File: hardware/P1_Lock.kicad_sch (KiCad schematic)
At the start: 5 parts, among them J1 Conn_01x07, U1 STM32L476RGTx

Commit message: Columns are 1-4
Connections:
- net at J1.4 (Pin_4): now also U1.41 (PA8)
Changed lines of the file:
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@@
+	(wire
+		(pts
+			(xy 144.78 74.93) (xy 152.4 74.93)
+		)
+		(stroke
+			(width 0)
+			(type default)
+		)
+	)
 	(wire
 		(pts
@@
 		(pts
 			(xy 187.96 107.95) (xy 160.02 107.95)
+		)
+		(stroke
+			(width 0)
+			(type default)
+		)
+	)
+	(wire
+		(pts
+			(xy 187.96 115.57) (xy 152.4 115.57)
 		)
 		(stroke
@@
 		)
 		(stroke
+			(width 0)
+			(type default)
+		)
+	)
+	(wire
+		(pts
+			(xy 152.4 115.57) (xy 152.4 74.93)
+		)
+		(stroke

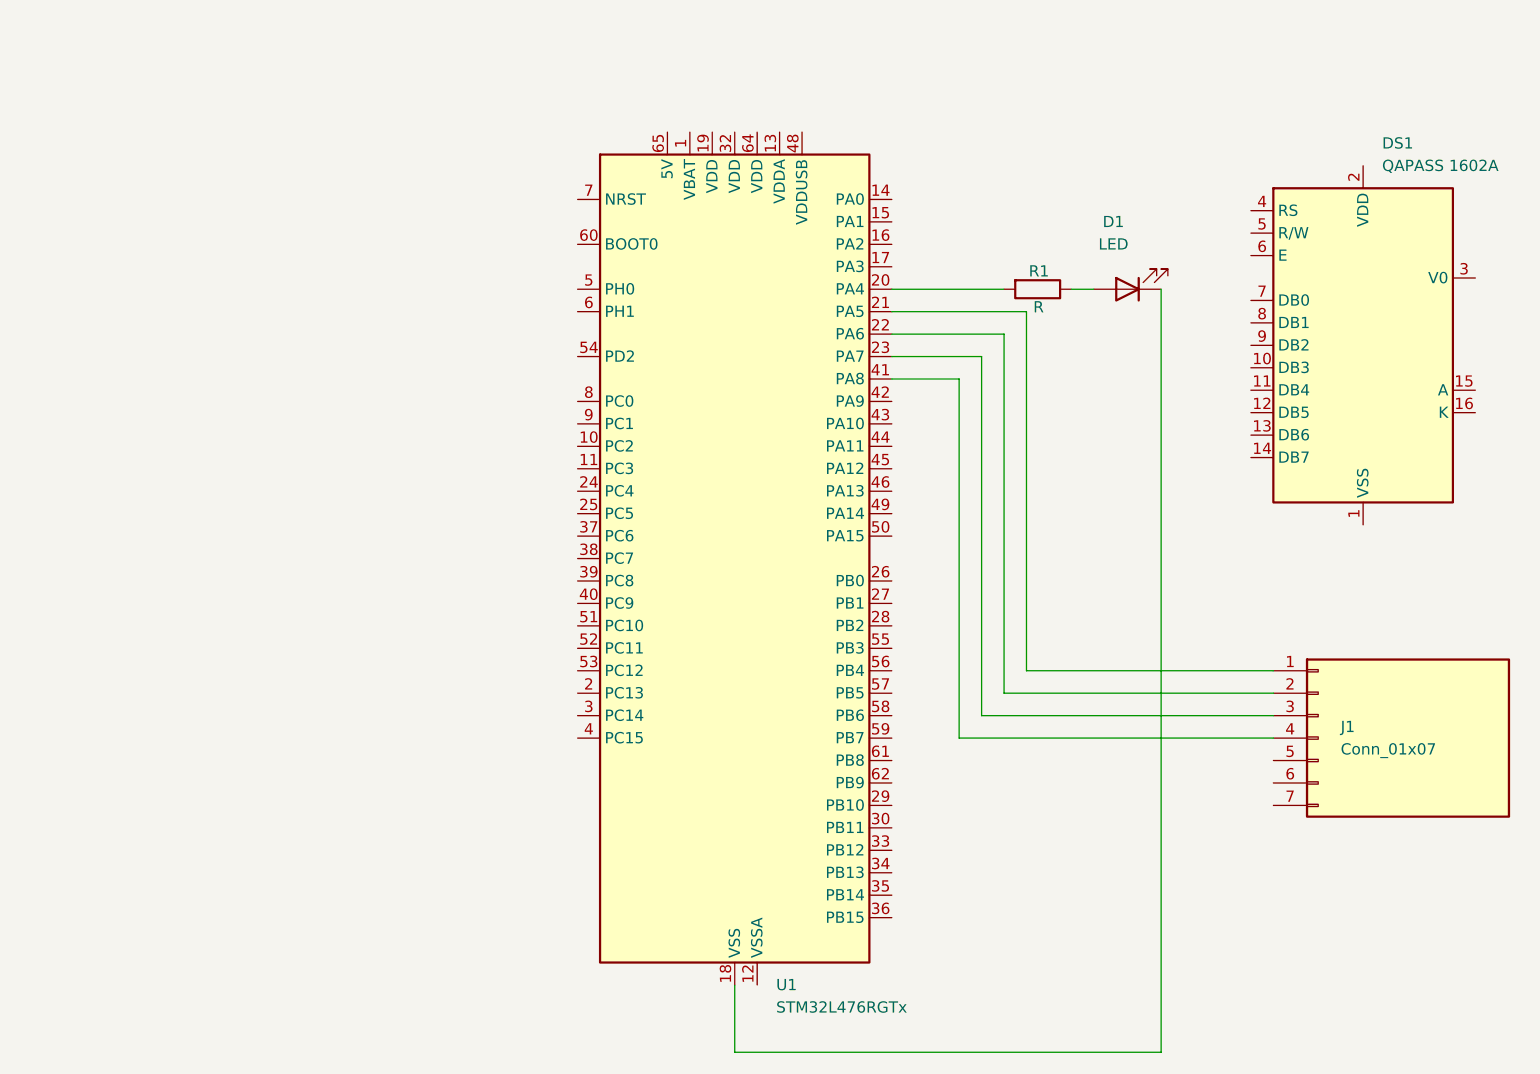
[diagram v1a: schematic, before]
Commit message: LCD Panel complete hooked up
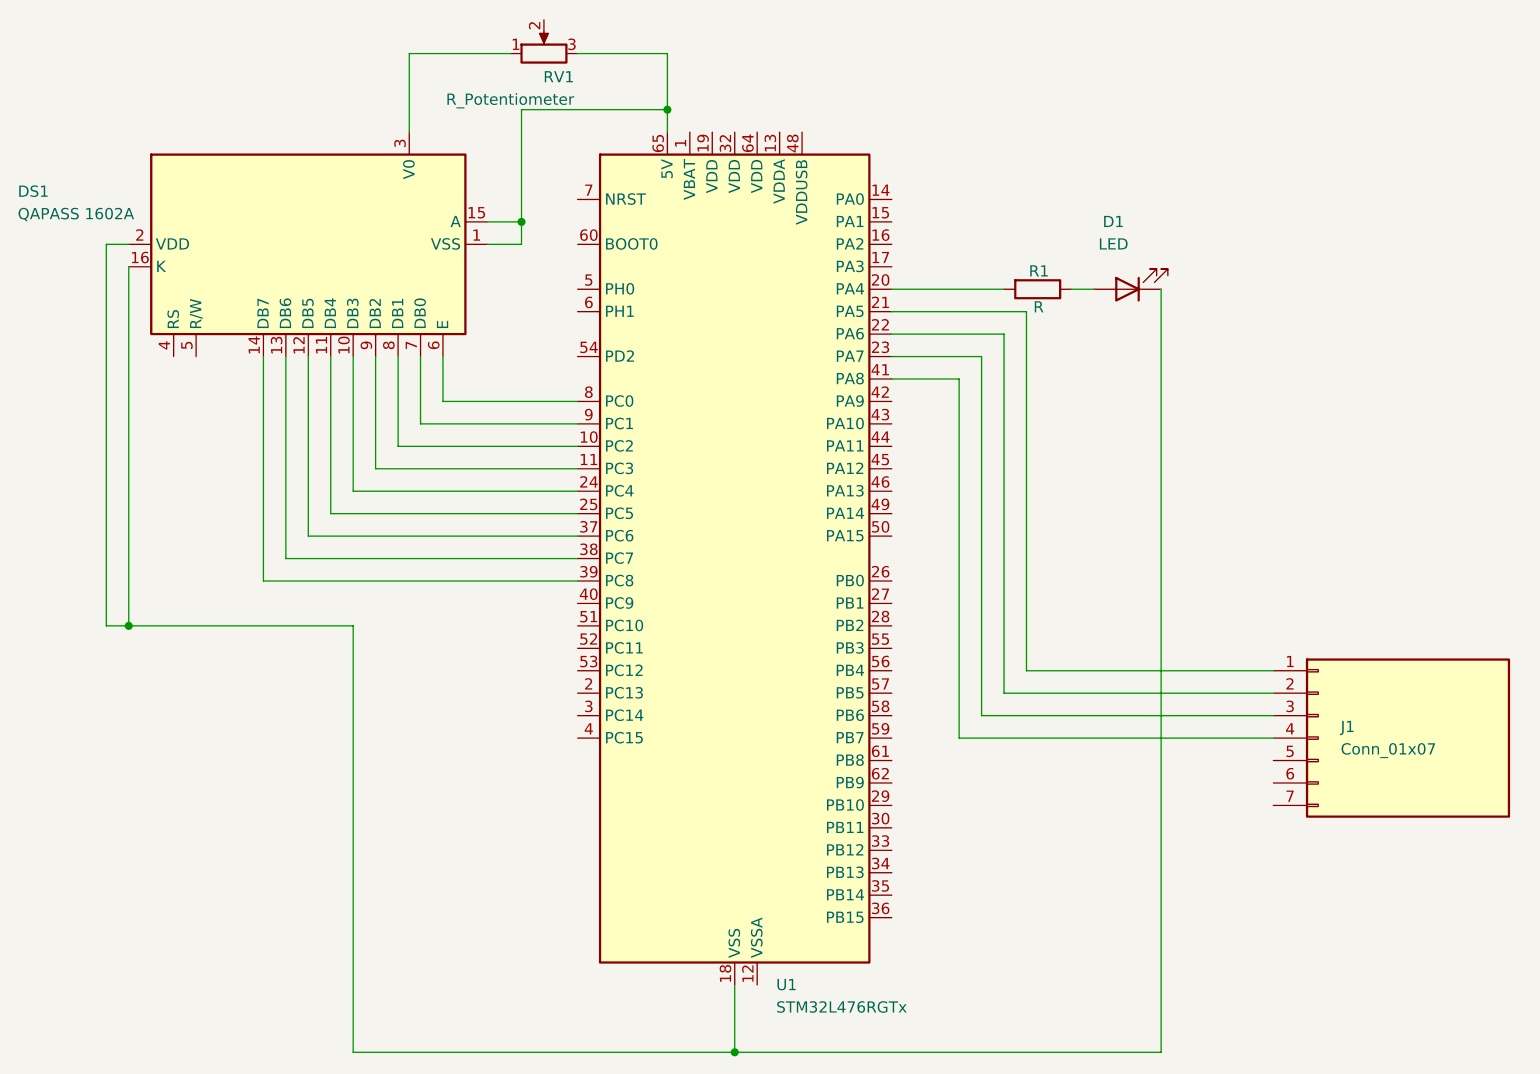
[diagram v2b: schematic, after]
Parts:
- added RV1: R_Potentiometer, symbol Device:R_Potentiometer
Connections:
- net at D1.1 (K), U1.18 (VSS), U1.31 (VSS)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: now also DS1.16 (K), DS1.2 (VDD)
- net at DS1.1 (VSS): now also DS1.15 (A), U1.65 (5V), RV1.3
- net at DS1.10 (DB3): now also U1.24 (PC4)
- net at DS1.11 (DB4): now also U1.25 (PC5)
- net at DS1.12 (DB5): now also U1.37 (PC6)
- net at DS1.13 (DB6): now also U1.38 (PC7)
- net at DS1.14 (DB7): now also U1.39 (PC8)
- net at DS1.3 (V0): now also RV1.1
- net at DS1.6 (E): now also U1.8 (PC0)
- net at DS1.7 (DB0): now also U1.9 (PC1)
- net at DS1.8 (DB1): now also U1.10 (PC2)
- net at DS1.9 (DB2): now also U1.11 (PC3)
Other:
- moved on the sheet: DS1
